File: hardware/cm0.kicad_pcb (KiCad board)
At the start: 4 copper layers, 85 x 56 mm, 252 parts, among them J1 USB_A_Stacked, J10 AudioJack_PJ-342, J2 USB_C_Receptacle_USB2.0_14P, J3 USB_C_Receptacle_USB2.0_14P, J4 USB_C_Receptacle_USB2.0_14P, J5 GPDI_A, J6 Micro_SD_Card_Det1, J7 RJ45_Hanrun_HR913550A_Horizon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, J8 Conn_01x03, J9 Conn_02x20_Odd_Even, Q1 BSN20, Q2 AO3415A, Q3 BSN20, Q4 BSN20, Q5 MMBT3904, U1 H3, U10 SY6280AAC, U11 SY6280AAC, U12 SY6280AAC, U13 TPD2EUSB30, U14 TPD2EUSB30, U15 TPD2EUSB30, U16 TPD2EUSB30, U17 HUSB237, U18 TPD2EUSB30, U19 UCL0524P, U2 H5TQ4G63EFR, U20 UCL0524P, U21 EMMC5.1_BGA153, U22 AP6212, U23 UCL0524P, U3 SY8088, U4 SY8088, U5 SY8088, U6 SY8089A, U7 SY8113, U8 SY8088, U9 SY6280AAC, Y1 32kHz, Y2 26MHz, Y3 24MHz

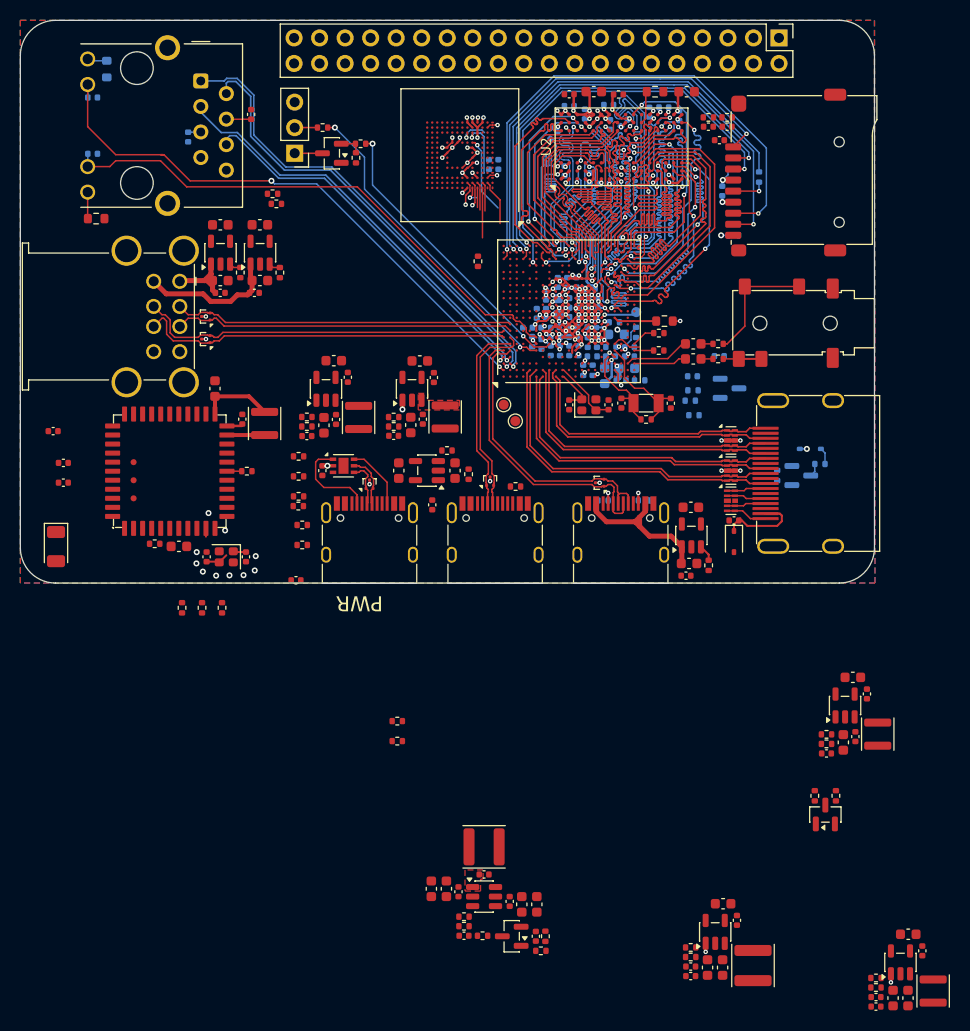
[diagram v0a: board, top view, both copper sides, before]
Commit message: Laid out the DCDC bucks
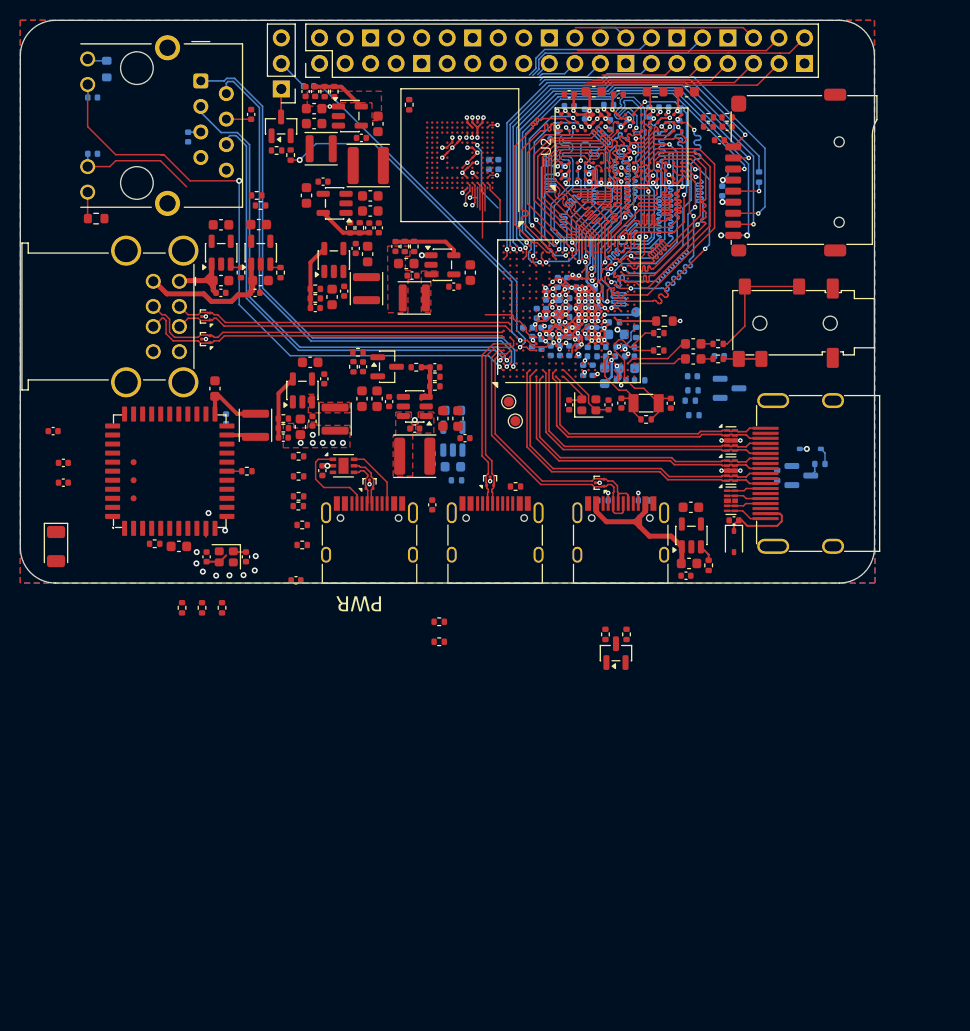
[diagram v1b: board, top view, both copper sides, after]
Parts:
- C105, C106, C113, R34, R36, R58, U12: moved to B.Cu
- J9: value Conn_02x20_Odd_Even -> GPIO
- moved C72 107.3 mm to (91.7, 94.2), turned to -90 degrees
- moved C71 106.0 mm to (92.6, 94.2), turned to 90 degrees
- moved C5 105.6 mm to (92.5, 95.9), turned to 0 degrees
- moved C73 105.2 mm to (92.5, 97.4), turned to 0 degrees
- moved R15 104.7 mm to (93.6, 94.2), turned to -90 degrees
- moved L3 103.6 mm to (93.2, 99.9), turned to 180 degrees
- moved R17 103.4 mm to (94.5, 94.2), turned to 90 degrees
- moved U5 100.5 mm to (96.1, 96.7), turned to 0 degrees
- moved C70 98.3 mm to (97.2, 98.8), turned to 0 degrees
- moved C69 96.4 mm to (98.9, 97.5), turned to 90 degrees
- moved L4 88.3 mm to (97.9, 101.6), turned to 0 degrees
- moved C79 84.4 mm to (98.1, 104.6), turned to 180 degrees
- moved C76 84.3 mm to (93.4, 103.2), turned to 180 degrees
- moved C80 82.4 mm to (98.1, 106.1), turned to 180 degrees
- moved U6 81.8 mm to (94.6, 105.4), turned to 180 degrees
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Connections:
- J9 pad 1: unconnected-(J9-Pin_1-Pad1) -> +3V3_IO
- J9 pad 14: unconnected-(J9-Pin_14-Pad14) -> GND
- J9 pad 2: unconnected-(J9-Pin_2-Pad2) -> +5V
- J9 pad 20: unconnected-(J9-Pin_20-Pad20) -> GND
- J9 pad 25: unconnected-(J9-Pin_25-Pad25) -> GND
- J9 pad 30: unconnected-(J9-Pin_30-Pad30) -> GND
- J9 pad 34: unconnected-(J9-Pin_34-Pad34) -> GND
- J9 pad 39: unconnected-(J9-Pin_39-Pad39) -> GND
- J9 pad 4: unconnected-(J9-Pin_4-Pad4) -> +5V
- J9 pad 6: unconnected-(J9-Pin_6-Pad6) -> GND
- J9 pad 9: unconnected-(J9-Pin_9-Pad9) -> GND
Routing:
- net /H3/SD_DET: track 0.00 -> 51.4 mm, vias 0 -> 2
- net /H3/EPHY_SPD_LED: track 53.9 -> 18.9 mm
- net unconnected-(J9-Pin_40-Pad40): track 0.00 -> 23.7 mm
- net unconnected-(J9-Pin_38-Pad38): track 0.00 -> 20.6 mm
- net unconnected-(J9-Pin_37-Pad37): track 0.00 -> 20.3 mm
- net unconnected-(J9-Pin_32-Pad32): track 0.00 -> 19.0 mm
- net unconnected-(J9-Pin_36-Pad36): track 0.00 -> 18.2 mm
- net unconnected-(J9-Pin_35-Pad35): track 0.00 -> 17.4 mm
- net unconnected-(J9-Pin_28-Pad28): track 0.00 -> 14.3 mm
- net unconnected-(J9-Pin_33-Pad33): track 0.00 -> 14.2 mm
- net unconnected-(J9-Pin_27-Pad27): track 0.00 -> 12.0 mm
- net unconnected-(J9-Pin_31-Pad31): track 0.00 -> 11.0 mm
- net /H3/EPHY_RX+: track 42.0 -> 50.8 mm
- net /H3/EPHY_RX-: track 38.2 -> 47.0 mm
- net /GPIO/CPU_RX: track 29.2 -> 37.9 mm
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- added copper zone on F.Cu, net +1V5
- added copper zone on F.Cu, net +3V3_AVCC
- added copper zone on F.Cu, net +3V3_WIFI
- added copper zone on F.Cu, net Net-(U3-LX)
- added copper zone on F.Cu, net Net-(U7-LX)

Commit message: Even more routing
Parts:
- removed C9: 100nF, Capacitor_SMD:C_0402_1005Metric
- added R71: 2k, Resistor_SMD:R_0402_1005Metric, F.Cu at (143.1, 150.2)
- added R72: 2k, Resistor_SMD:R_0402_1005Metric, F.Cu at (143.1, 152.2)
- C114, R10, R11, R51, R69: moved to B.Cu
- D1, Q3, R37, R38: moved to F.Cu
- moved R10 32.0 mm to (108.8, 115.2), turned to -90 degrees
- moved R70 22.4 mm to (70.9, 127.0)
- moved C105 21.0 mm to (112.2, 151.7)
- moved C106 21.0 mm to (112.2, 146.1)
- moved R34 21.0 mm to (112.6, 153.1)
- moved R36 21.0 mm to (110.2, 150.9)
- moved U12 21.0 mm to (112.2, 148.9)
- moved R7 19.8 mm to (132.0, 116.5), turned to -90 degrees
- moved C42 18.9 mm to (131.1, 116.5), turned to 90 degrees
- moved R8 17.8 mm to (132.0, 114.6), turned to -90 degrees
- moved C43 16.9 mm to (131.1, 114.6), turned to 90 degrees
- moved C114 16.5 mm to (82.1, 128.8), turned to -135 degrees
- moved R51 14.3 mm to (85.9, 132.8)
- moved D1 12.3 mm to (130.3, 125.9), turned to 90 degrees
- moved R38 12.0 mm to (131.8, 126.8), turned to 90 degrees
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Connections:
- D1 pad 2: +3V3 -> +3V3_IO
- Q3 pad 1: +3V3 -> +3V3_IO
- R37 pad 1: +3V3 -> +3V3_IO
- U1 pad B1: unconnected-(U1C-PG13-PadB1) -> /H3/WL_REG_ON
- U1 pad F13: /H3/WL_REG_ON -> unconnected-(U1F-PA8-PadF13)
- U1 pad V2: unconnected-(U1F-PL10-PadV2) -> /H3/PWR_LED
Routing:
- net /H3/BT_TXD: track 0.00 -> 49.2 mm, vias 0 -> 2
- net /H3/BT_HOST_WAKE: track 0.00 -> 49.2 mm, vias 0 -> 2
- net /H3/~{BT_CTS}: track 0.00 -> 49.0 mm, vias 0 -> 2
- net /H3/WIFI_32K: track 0.00 -> 48.9 mm, vias 0 -> 2
- net /H3/BT_RXD: track 0.06 -> 47.9 mm, vias 0 -> 2
- net /H3/~{BT_RTS}: track 0.00 -> 46.1 mm, vias 0 -> 2
- net /H3/WL_HOST_WAKE: track 0.00 -> 45.1 mm, vias 0 -> 2
- net /H3/WL_REG_ON: track 0.00 -> 43.2 mm, vias 0 -> 2
- net /H3/SDIO_D2: track 0.00 -> 42.4 mm, vias 0 -> 2
- net /H3/SDIO_D3: track 0.00 -> 40.2 mm, vias 0 -> 2
- net /H3/SDIO_CMD: track 0.00 -> 39.9 mm, vias 0 -> 2
- net /H3/SDIO_D0: track 0.00 -> 37.5 mm, vias 0 -> 2
- net /H3/SDIO_D1: track 0.00 -> 35.5 mm, vias 0 -> 2
- net /H3/SDIO_CLK: track 0.00 -> 35.4 mm, vias 0 -> 2
- net /GPDI/GPDI_SCL: track 3.95 -> 27.6 mm, vias 0 -> 2
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- added copper zone on B.Cu, net /H3/AGND
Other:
- board text added: "Low speed USB comms"
